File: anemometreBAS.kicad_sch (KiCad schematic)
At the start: 12 parts, among them J1 Conn_01x03_Male, J2 Conn_01x02_Male, J3 Conn_01x02_Male, J4 Conn_01x02_Male, J5 Conn_01x02_Male, U1 TP4056

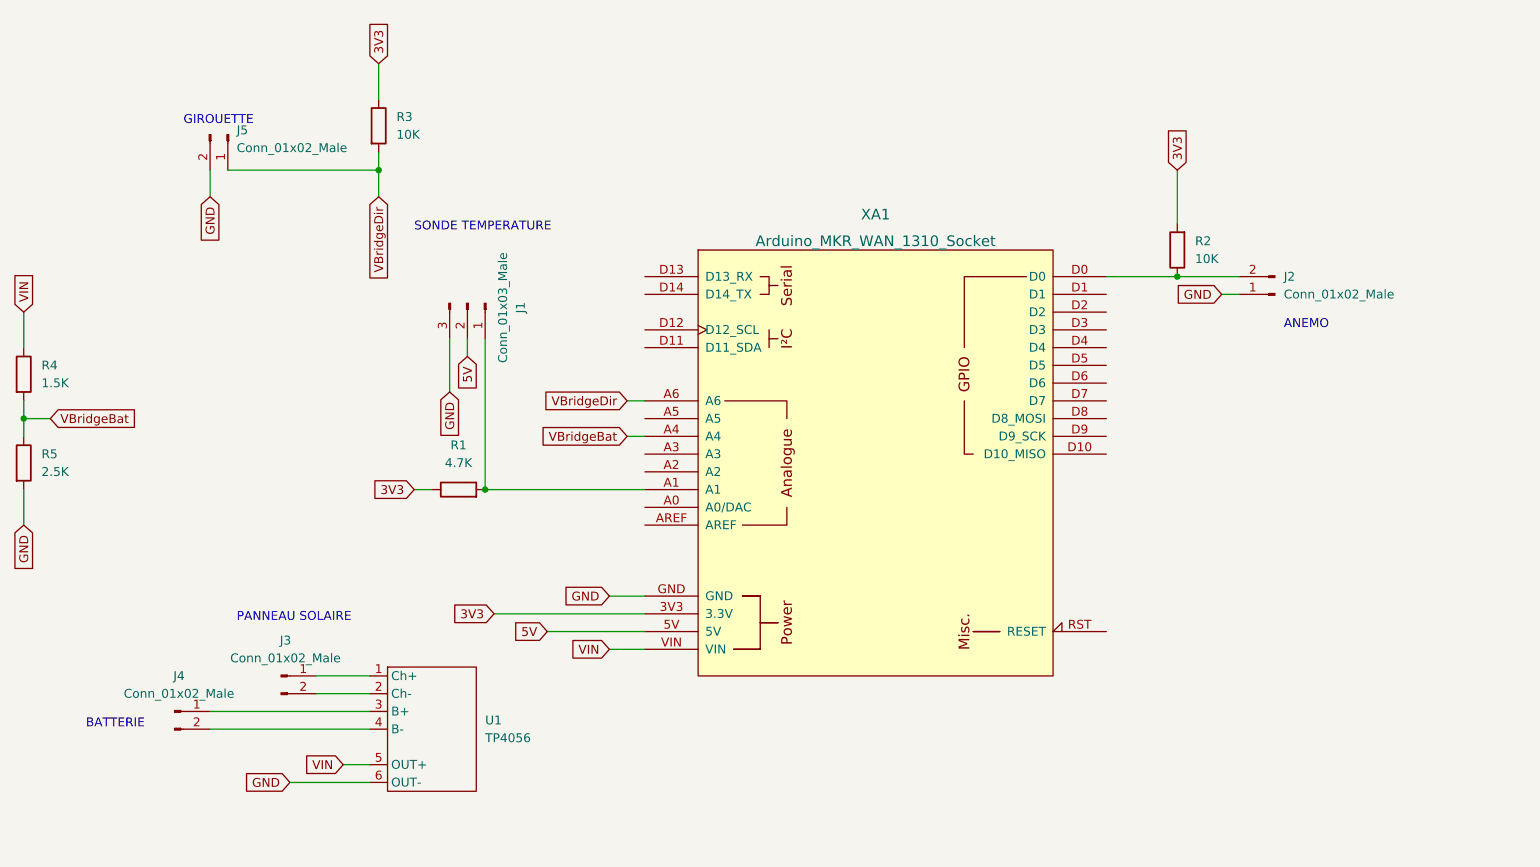
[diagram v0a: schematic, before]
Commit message: first pcb version with schematic footprint update
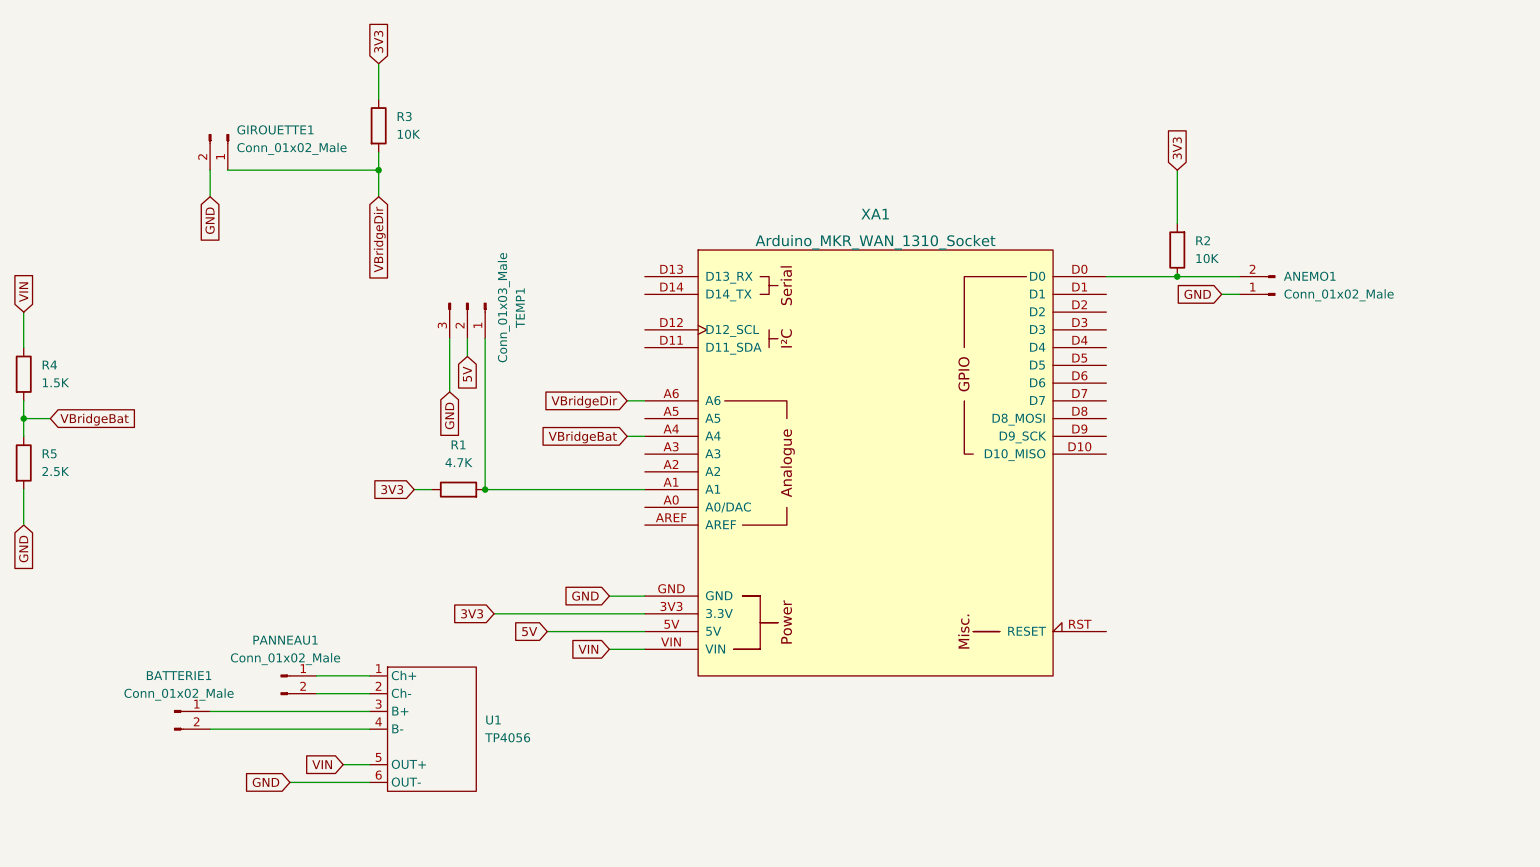
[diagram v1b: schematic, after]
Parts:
- ANEMO1: renamed from J2; footprint (none) -> Connector_JST:JST_XH_B3B-XH-A_1x03_P2.50mm_Vertical
- BATTERIE1: renamed from J4; footprint (none) -> Connector_JST:JST_XH_B2B-XH-A_1x02_P2.50mm_Vertical
- GIROUETTE1: renamed from J5; footprint (none) -> Connector_JST:JST_XH_B3B-XH-A_1x03_P2.50mm_Vertical
- PANNEAU1: renamed from J3; footprint (none) -> Connector_JST:JST_XH_B2B-XH-A_1x02_P2.50mm_Vertical
- R1, R2, R3, R4, R5: footprint (none) -> Resistor_SMD:R_0805_2012Metric_Pad1.20x1.40mm_HandSolder
- TEMP1: renamed from J1; footprint (none) -> Connector_JST:JST_XH_B3B-XH-A_1x03_P2.50mm_Vertical
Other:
- note removed: "ANEMO"
- note removed: "BATTERIE"
- note removed: "GIROUETTE"
- note removed: "PANNEAU SOLAIRE"
- note removed: "SONDE TEMPERATURE"
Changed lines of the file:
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@@
     (stroke (width 0) (type default) (color 0 0 0 0))
-  )
-  (text "GIROUETTE" (at 57.15 34.29 0)
-    (effects (font (size 1.27 1.27)) (justify left bottom))
-  )
-  (text "SONDE TEMPERATURE" (at 90.17 49.53 0)
-    (effects (font (size 1.27 1.27)) (justify left bottom))
-  )
-  (text "ANEMO" (at 214.63 63.5 0)
-    (effects (font (size 1.27 1.27)) (justify left bottom))
-  )
-  (text "PANNEAU SOLAIRE" (at 64.77 105.41 0)
-    (effects (font (size 1.27 1.27)) (justify left bottom))
-  )
-  (text "BATTERIE" (at 43.18 120.65 0)
-    (effects (font (size 1.27 1.27)) (justify left bottom))
   )
   (global_label "VBridgeDir" (shape input) (at 85.09 44.45 270) (fields_autoplaced)
@@
   (symbol (lib_id "Connector:Conn_01x02_Male") (at 55.88 118.11 0) (unit 1)
     (in_bom yes) (on_board yes) (fields_autoplaced)
-    (property "Reference" "J4" (id 0) (at 56.515 113.03 0))
+    (property "Reference" "BATTERIE1" (id 0) (at 56.515 113.03 0))
     (property "Value" "Conn_01x02_Male" (id 1) (at 56.515 115.57 0))
-    (property "Footprint" "" (id 2) (at 55.88 118.11 0)
+    (property "Footprint" "Connector_JST:JST_XH_B2B-XH-A_1x02_P2.50mm_Vertical" (id 2) (at 55.88 118.11 0)
       (effects (font (size 1.27 1.27)) hide)
     )
@@
       (effects (font (size 1.27 1.27)) (justify left))
     )
-    (property "Footprint" "" (id 2) (at 32.512 69.85 90)
+    (property "Footprint" "Resistor_SMD:R_0805_2012Metric_Pad1.20x1.40mm_HandSolder" (id 2) (at 32.512 69.85 90)
       (effects (font (size 1.27 1.27)) hide)
     )
@@
   (symbol (lib_id "Connector:Conn_01x02_Male") (at 71.12 113.03 0) (unit 1)
     (in_bom yes) (on_board yes)
-    (property "Reference" "J3" (id 0) (at 71.755 107.95 0))
+    (property "Reference" "PANNEAU1" (id 0) (at 71.755 107.95 0))
     (property "Value" "Conn_01x02_Male" (id 1) (at 71.755 110.49 0))
-    (property "Footprint" "" (id 2) (at 71.12 113.03 0)
+    (property "Footprint" "Connector_JST:JST_XH_B2B-XH-A_1x02_P2.50mm_Vertical" (id 2) (at 71.12 113.03 0)
       (effects (font (size 1.27 1.27)) hide)
     )
@@
   (symbol (lib_id "Connector:Conn_01x02_Male") (at 63.5 35.56 270) (unit 1)
     (in_bom yes) (on_board yes) (fields_autoplaced)
-    (property "Reference" "J5" (id 0) (at 64.77 34.9249 90)
+    (property "Reference" "GIROUETTE1" (id 0) (at 64.77 34.9249 90)
       (effects (font (size 1.27 1.27)) (justify left))
     )
@@
       (effects (font (size 1.27 1.27)) (justify left))
     )
-    (property "Footprint" "" (id 2) (at 63.5 35.56 0)
+    (property "Footprint" "Connector_JST:JST_XH_B3B-XH-A_1x03_P2.50mm_Vertical" (id 2) (at 63.5 35.56 0)
       (effects (font (size 1.27 1.27)) hide)
     )
@@
   (symbol (lib_id "Connector:Conn_01x03_Male") (at 97.79 59.69 270) (unit 1)
     (in_bom yes) (on_board yes)
-    (property "Reference" "J1" (id 0) (at 105.41 60.325 0))
+    (property "Reference" "TEMP1" (id 0) (at 105.41 60.325 0))
     (property "Value" "Conn_01x03_Male" (id 1) (at 102.87 60.325 0))
-    (property "Footprint" "" (id 2) (at 97.79 59.69 0)
+    (property "Footprint" "Connector_JST:JST_XH_B3B-XH-A_1x03_P2.50mm_Vertical" (id 2) (at 97.79 59.69 0)
       (effects (font (size 1.27 1.27)) hide)
     )
@@
       (effects (font (size 1.27 1.27)) (justify left))
     )
-    (property "Footprint" "" (id 2) (at 32.512 82.55 90)
+    (property "Footprint" "Resistor_SMD:R_0805_2012Metric_Pad1.20x1.40mm_HandSolder" (id 2) (at 32.512 82.55 90)
       (effects (font (size 1.27 1.27)) hide)
     )
@@
       (effects (font (size 1.27 1.27)) (justify left))
     )
-    (property "Footprint" "" (id 2) (at 83.312 34.29 90)
+    (property "Footprint" "Resistor_SMD:R_0805_2012Metric_Pad1.20x1.40mm_HandSolder" (id 2) (at 83.312 34.29 90)
       (effects (font (size 1.27 1.27)) hide)
     )
@@
   (symbol (lib_id "Connector:Conn_01x02_Male") (at 213.36 58.42 180) (unit 1)
     (in_bom yes) (on_board yes) (fields_autoplaced)
-    (property "Reference" "J2" (id 0) (at 214.63 55.8799 0)
+    (property "Reference" "ANEMO1" (id 0) (at 214.63 55.8799 0)
       (effects (font (size 1.27 1.27)) (justify right))
     )
@@
       (effects (font (size 1.27 1.27)) (justify right))
     )
-    (property "Footprint" "" (id 2) (at 213.36 58.42 0)
+    (property "Footprint" "Connector_JST:JST_XH_B3B-XH-A_1x03_P2.50mm_Vertical" (id 2) (at 213.36 58.42 0)
       (effects (font (size 1.27 1.27)) hide)
     )
@@
     (property "Reference" "R1" (id 0) (at 96.52 80.01 90))
     (property "Value" "4.7K" (id 1) (at 96.52 82.55 90))
-    (property "Footprint" "" (id 2) (at 96.52 88.138 90)
+    (property "Footprint" "Resistor_SMD:R_0805_2012Metric_Pad1.20x1.40mm_HandSolder" (id 2) (at 96.52 88.138 90)
       (effects (font (size 1.27 1.27)) hide)
     )
@@
       (effects (font (size 1.27 1.27)) (justify right))
     )
-    (property "Footprint" "" (id 2) (at 201.168 52.07 90)
+    (property "Footprint" "Resistor_SMD:R_0805_2012Metric_Pad1.20x1.40mm_HandSolder" (id 2) (at 201.168 52.07 90)
       (effects (font (size 1.27 1.27)) hide)
     )
@@
   )
   (symbol_instances
+    (path "/9f0685af-69ed-4dea-80ce-436dc1fe9397"
+      (reference "ANEMO1") (unit 1) (value "Conn_01x02_Male") (footprint "Connector_JST:JST_XH_B3B-XH-A_1x03_P2.50mm_Vertical")
+    )
+    (path "/1ebde9b6-36d2-4ec2-927a-d7b79a686a71"
+      (reference "BATTERIE1") (unit 1) (value "Conn_01x02_Male") (footprint "Connector_JST:JST_XH_B2B-XH-A_1x02_P2.50mm_Vertical")
+    )
+    (path "/63e0ab31-586b-47af-b3e0-5d58db250f77"
+      (reference "GIROUETTE1") (unit 1) (value "Conn_01x02_Male") (footprint "Connector_JST:JST_XH_B3B-XH-A_1x03_P2.50mm_Vertical")
+    )
+    (path "/3c744949-20c9-495f-819b-b231fc469afd"
+      (reference "PANNEAU1") (unit 1) (value "Conn_01x02_Male") (footprint "Connector_JST:JST_XH_B2B-XH-A_1x02_P2.50mm_Vertical")
+    )
+    (path "/f940d3df-5e0a-4d9e-b355-0a70feea90ed"
+      (reference "R1") (unit 1) (value "4.7K") (footprint "Resistor_SMD:R_0805_2012Metric_Pad1.20x1.40mm_HandSolder")
+    )
+    (path "/fe70beb6-5a5d-44ad-9cb0-b8140f5733f6"
+      (reference "R2") (unit 1) (value "10K") (footprint "Resistor_SMD:R_0805_2012Metric_Pad1.20x1.40mm_HandSolder")
+    )
+    (path "/7ff684fb-0f57-4268-90ca-eb7a837149a2"
+      (reference "R3") (unit 1) (value "10K") (footprint "Resistor_SMD:R_0805_2012Metric_Pad1.20x1.40mm_HandSolder")
+    )
+    (path "/27703255-477e-4db9-96c9-2aada29d5b52"
+      (reference "R4") (unit 1) (value "1.5K") (footprint "Resistor_SMD:R_0805_2012Metric_Pad1.20x1.40mm_HandSolder")
+    )
+    (path "/74681689-b7a9-42ae-980c-5f12c8a445bb"
+      (reference "R5") (unit 1) (value "2.5K") (footprint "Resistor_SMD:R_0805_2012Metric_Pad1.20x1.40mm_HandSolder")
+    )
     (path "/72bc82b9-9a1c-4c01-af38-f3cc7938766f"
-      (reference "J1") (unit 1) (value "Conn_01x03_Male") (footprint "")
-    )
-    (path "/9f0685af-69ed-4dea-80ce-436dc1fe9397"
-      (reference "J2") (unit 1) (value "Conn_01x02_Male") (footprint "")
-    )
-    (path "/3c744949-20c9-495f-819b-b231fc469afd"
-      (reference "J3") (unit 1) (value "Conn_01x02_Male") (footprint "")
-    )
-    (path "/1ebde9b6-36d2-4ec2-927a-d7b79a686a71"
-      (reference "J4") (unit 1) (value "Conn_01x02_Male") (footprint "")
-    )
-    (path "/63e0ab31-586b-47af-b3e0-5d58db250f77"
-      (reference "J5") (unit 1) (value "Conn_01x02_Male") (footprint "")
-    )
-    (path "/f940d3df-5e0a-4d9e-b355-0a70feea90ed"
-      (reference "R1") (unit 1) (value "4.7K") (footprint "")
-    )
-    (path "/fe70beb6-5a5d-44ad-9cb0-b8140f5733f6"
-      (reference "R2") (unit 1) (value "10K") (footprint "")
-    )
-    (path "/7ff684fb-0f57-4268-90ca-eb7a837149a2"
-      (reference "R3") (unit 1) (value "10K") (footprint "")
-    )
-    (path "/27703255-477e-4db9-96c9-2aada29d5b52"
-      (reference "R4") (unit 1) (value "1.5K") (footprint "")
-    )
-    (path "/74681689-b7a9-42ae-980c-5f12c8a445bb"
-      (reference "R5") (unit 1) (value "2.5K") (footprint "")
+      (reference "TEMP1") (unit 1) (value "Conn_01x03_Male") (footprint "Connector_JST:JST_XH_B3B-XH-A_1x03_P2.50mm_Vertical")
     )
     (path "/0631378f-d2b8-46a0-905a-76481eb8111b"

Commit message: schematic 	GND at the same pin for each connector 	add M3 hole*3 connected to GND PCB 	first routing
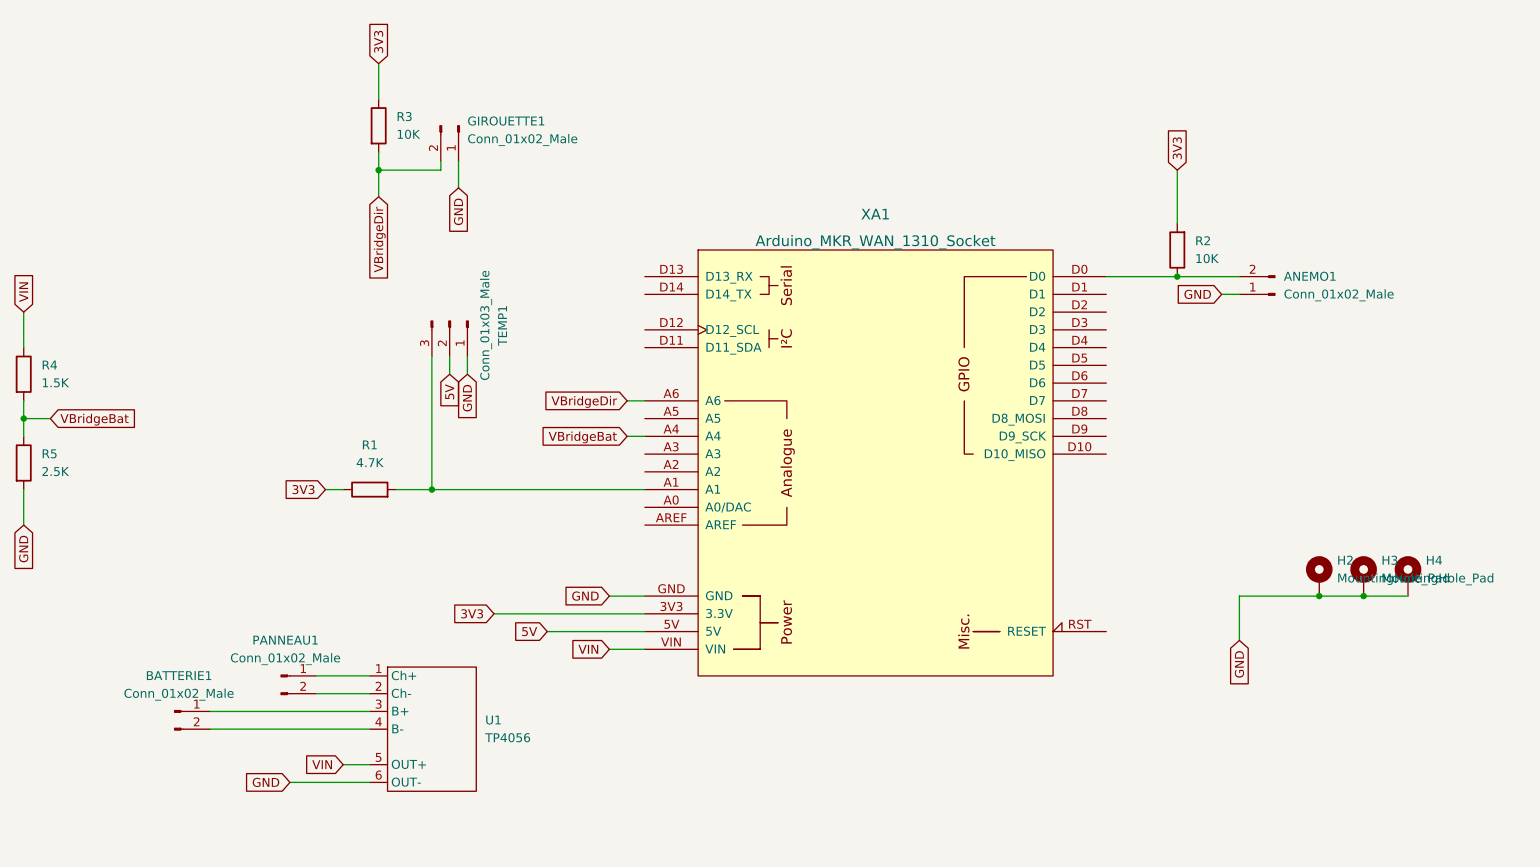
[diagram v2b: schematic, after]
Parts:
- added H2, H3, H4: MountingHole_Pad, MountingHole:MountingHole_3.2mm_M3_Pad_TopBottom, symbol Mechanical:MountingHole_Pad
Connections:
- net GND: now also GIROUETTE1.1 (Pin_1), TEMP1.1 (Pin_1), H2.1, H3.1, H4.1; no longer GIROUETTE1.2 (Pin_2), TEMP1.3 (Pin_3)
- net VBridgeDir: now also GIROUETTE1.2 (Pin_2); no longer GIROUETTE1.1 (Pin_1)
- net at R1.2, XA1.A1: now also TEMP1.3 (Pin_3); no longer TEMP1.1 (Pin_1)
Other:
- moved on the sheet: GIROUETTE1, R1, TEMP1

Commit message: pcb without smd resistor first routing version
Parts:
- R1, R2, R3, R4, R5: footprint Resistor_SMD:R_0805_2012Metric_Pad1.20x1.40mm_HandSolder -> Resistor_THT:R_Axial_DIN0204_L3.6mm_D1.6mm_P7.62mm_Horizontal
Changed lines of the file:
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@@
       (effects (font (size 1.27 1.27)) (justify left))
     )
-    (property "Footprint" "Resistor_SMD:R_0805_2012Metric_Pad1.20x1.40mm_HandSolder" (id 2) (at 32.512 69.85 90)
+    (property "Footprint" "Resistor_THT:R_Axial_DIN0204_L3.6mm_D1.6mm_P7.62mm_Horizontal" (id 2) (at 32.512 69.85 90)
       (effects (font (size 1.27 1.27)) hide)
     )
@@
       (effects (font (size 1.27 1.27)) (justify left))
     )
-    (property "Footprint" "Resistor_SMD:R_0805_2012Metric_Pad1.20x1.40mm_HandSolder" (id 2) (at 32.512 82.55 90)
+    (property "Footprint" "Resistor_THT:R_Axial_DIN0204_L3.6mm_D1.6mm_P7.62mm_Horizontal" (id 2) (at 32.512 82.55 90)
       (effects (font (size 1.27 1.27)) hide)
     )
@@
       (effects (font (size 1.27 1.27)) (justify left))
     )
-    (property "Footprint" "Resistor_SMD:R_0805_2012Metric_Pad1.20x1.40mm_HandSolder" (id 2) (at 83.312 34.29 90)
+    (property "Footprint" "Resistor_THT:R_Axial_DIN0204_L3.6mm_D1.6mm_P7.62mm_Horizontal" (id 2) (at 83.312 34.29 90)
       (effects (font (size 1.27 1.27)) hide)
     )
@@
     (property "Reference" "R1" (id 0) (at 83.82 80.01 90))
     (property "Value" "4.7K" (id 1) (at 83.82 82.55 90))
-    (property "Footprint" "Resistor_SMD:R_0805_2012Metric_Pad1.20x1.40mm_HandSolder" (id 2) (at 83.82 88.138 90)
+    (property "Footprint" "Resistor_THT:R_Axial_DIN0204_L3.6mm_D1.6mm_P7.62mm_Horizontal" (id 2) (at 83.82 88.138 90)
       (effects (font (size 1.27 1.27)) hide)
     )
@@
       (effects (font (size 1.27 1.27)) (justify right))
     )
-    (property "Footprint" "Resistor_SMD:R_0805_2012Metric_Pad1.20x1.40mm_HandSolder" (id 2) (at 201.168 52.07 90)
+    (property "Footprint" "Resistor_THT:R_Axial_DIN0204_L3.6mm_D1.6mm_P7.62mm_Horizontal" (id 2) (at 201.168 52.07 90)
       (effects (font (size 1.27 1.27)) hide)
     )
@@
     )
     (path "/f940d3df-5e0a-4d9e-b355-0a70feea90ed"
-      (reference "R1") (unit 1) (value "4.7K") (footprint "Resistor_SMD:R_0805_2012Metric_Pad1.20x1.40mm_HandSolder")
+      (reference "R1") (unit 1) (value "4.7K") (footprint "Resistor_THT:R_Axial_DIN0204_L3.6mm_D1.6mm_P7.62mm_Horizontal")
     )
     (path "/fe70beb6-5a5d-44ad-9cb0-b8140f5733f6"
-      (reference "R2") (unit 1) (value "10K") (footprint "Resistor_SMD:R_0805_2012Metric_Pad1.20x1.40mm_HandSolder")
+      (reference "R2") (unit 1) (value "10K") (footprint "Resistor_THT:R_Axial_DIN0204_L3.6mm_D1.6mm_P7.62mm_Horizontal")
     )
     (path "/7ff684fb-0f57-4268-90ca-eb7a837149a2"
-      (reference "R3") (unit 1) (value "10K") (footprint "Resistor_SMD:R_0805_2012Metric_Pad1.20x1.40mm_HandSolder")
+      (reference "R3") (unit 1) (value "10K") (footprint "Resistor_THT:R_Axial_DIN0204_L3.6mm_D1.6mm_P7.62mm_Horizontal")
     )
     (path "/27703255-477e-4db9-96c9-2aada29d5b52"
-      (reference "R4") (unit 1) (value "1.5K") (footprint "Resistor_SMD:R_0805_2012Metric_Pad1.20x1.40mm_HandSolder")
+      (reference "R4") (unit 1) (value "1.5K") (footprint "Resistor_THT:R_Axial_DIN0204_L3.6mm_D1.6mm_P7.62mm_Horizontal")
     )
     (path "/74681689-b7a9-42ae-980c-5f12c8a445bb"
-      (reference "R5") (unit 1) (value "2.5K") (footprint "Resistor_SMD:R_0805_2012Metric_Pad1.20x1.40mm_HandSolder")
+      (reference "R5") (unit 1) (value "2.5K") (footprint "Resistor_THT:R_Axial_DIN0204_L3.6mm_D1.6mm_P7.62mm_Horizontal")
     )
     (path "/72bc82b9-9a1c-4c01-af38-f3cc7938766f"
